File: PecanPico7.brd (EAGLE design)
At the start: 34.2 x 50 mm, 178 parts, among them IC1 Si4060-B1B-FM, IC10 TPS62260DRVT, IC11 TPS62261DRVT, IC12 TPS63021, IC13 RF6886, IC14 TPS78227DDCR, IC16 PAC1720-1-AIA-TR, IC2 Si4060-B1B-FM, IC3 BME280_BME280, IC4 uBlox MAX7/8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

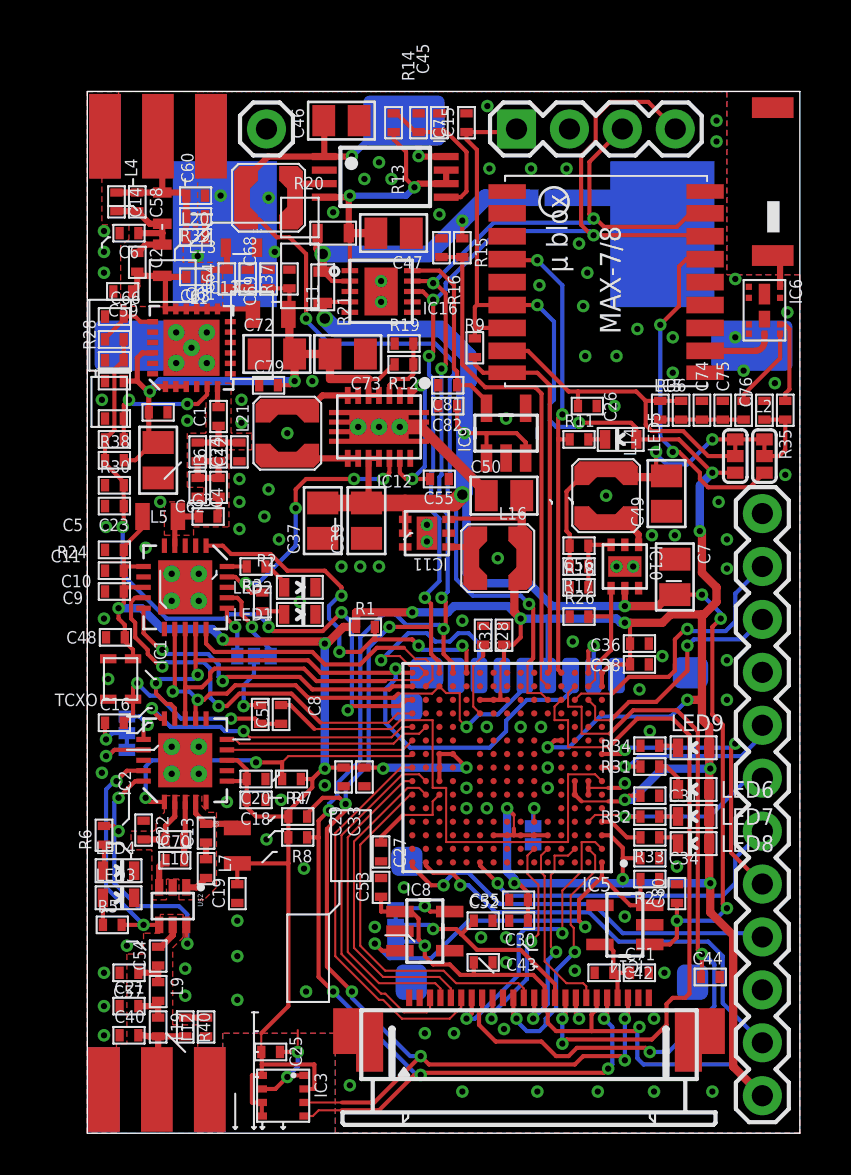
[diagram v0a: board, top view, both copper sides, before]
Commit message: Replaced small TCXO package to larger one
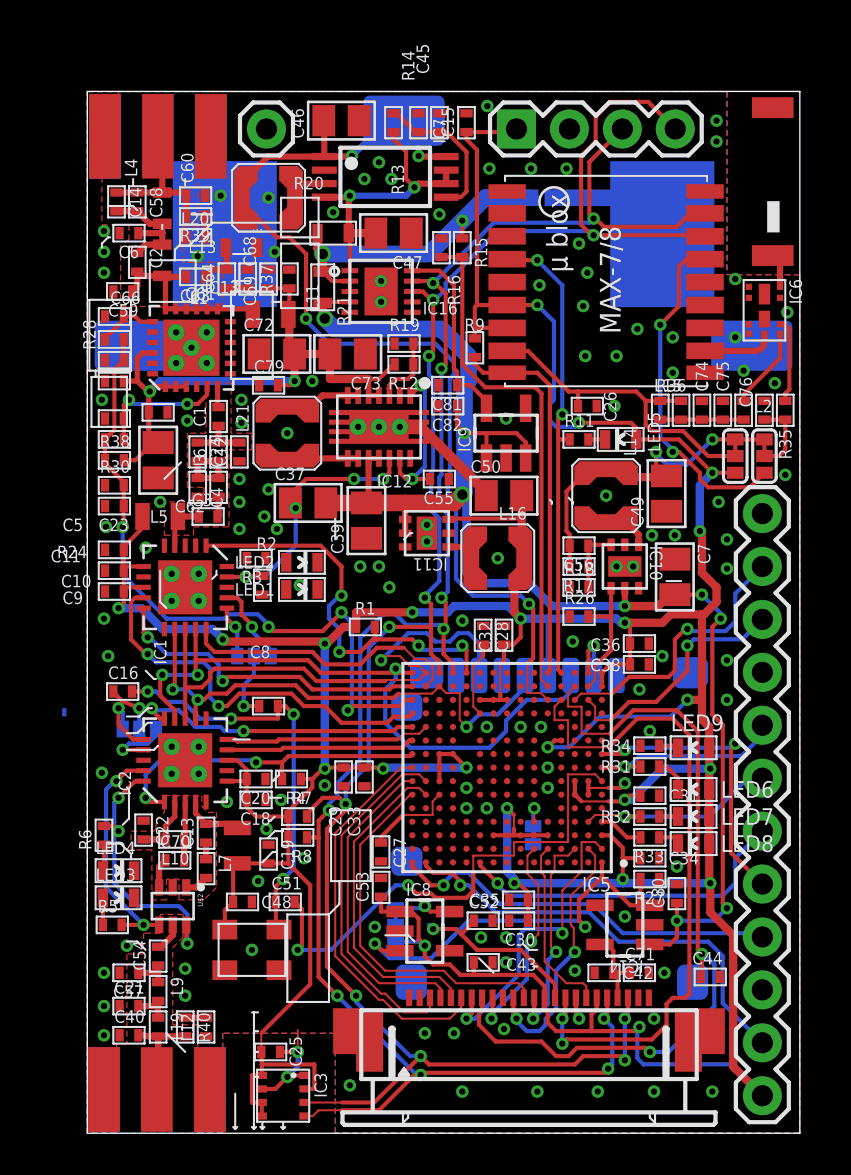
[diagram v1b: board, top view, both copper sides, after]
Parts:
- removed TCXO: KT2016K2BCW18ZAS, PecanFemto3:TCXO_2.0X1.6
- added U$3: TXC_7Z7Q, PecanFemto3:TCXO_3.2X2.5
- moved C48 14.1 mm to (7.45, 11.1), turned to 0 degrees
- moved C51 9.00 mm to (9.50, 11.1), turned to 0 degrees
- moved C19 2.42 mm to (8.70, 13.4), turned to 270 degrees
- moved C16 1.55 mm to (1.70, 21.2)
- moved LED1 1.20 mm to (10.3, 26.1)
- moved LED2 1.20 mm to (10.3, 27.4)
- moved C37 1.10 mm to (10.6, 30.2), turned to 0 degrees
- moved R2 0.80 mm to (8.40, 26.3)
- moved SJ6 0.63 mm to (2.50, 19.4), turned to 180 degrees
- moved C8 0.57 mm to (8.70, 20.5), turned to 0 degrees
- moved R3 0.40 mm to (8.10, 27.6)
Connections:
- net CLOCK: now also U$3.3; no longer TCXO.3
- net GND: now also U$3.1, U$3.2; no longer TCXO.1, TCXO.2
- net VCC: now also U$3.4; no longer TCXO.4
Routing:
- net CLOCK: track 9.88 -> 19.9 mm, vias 2 -> 4
- net CAM_VCC_CORE: track 10.4 -> 8.78 mm
- net N$22: track 1.46 -> 0.00 mm
- net N$19: track 1.95 -> 3.37 mm
- net N$21: track 1.20 -> 0.00 mm
- net N$13: track 0.95 -> 0.00 mm
- net N$39: track 25.3 -> 24.5 mm, vias 0 -> 2
- net VCC: track 250.2 -> 250.9 mm
- net RADIO1_SDN: track 19.4 -> 19.9 mm
- net N$34: track 1.94 -> 2.52 mm
- net PA_EN: track 13.5 -> 13.0 mm
- net GND: vias 123 -> 120

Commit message: Moved parts around
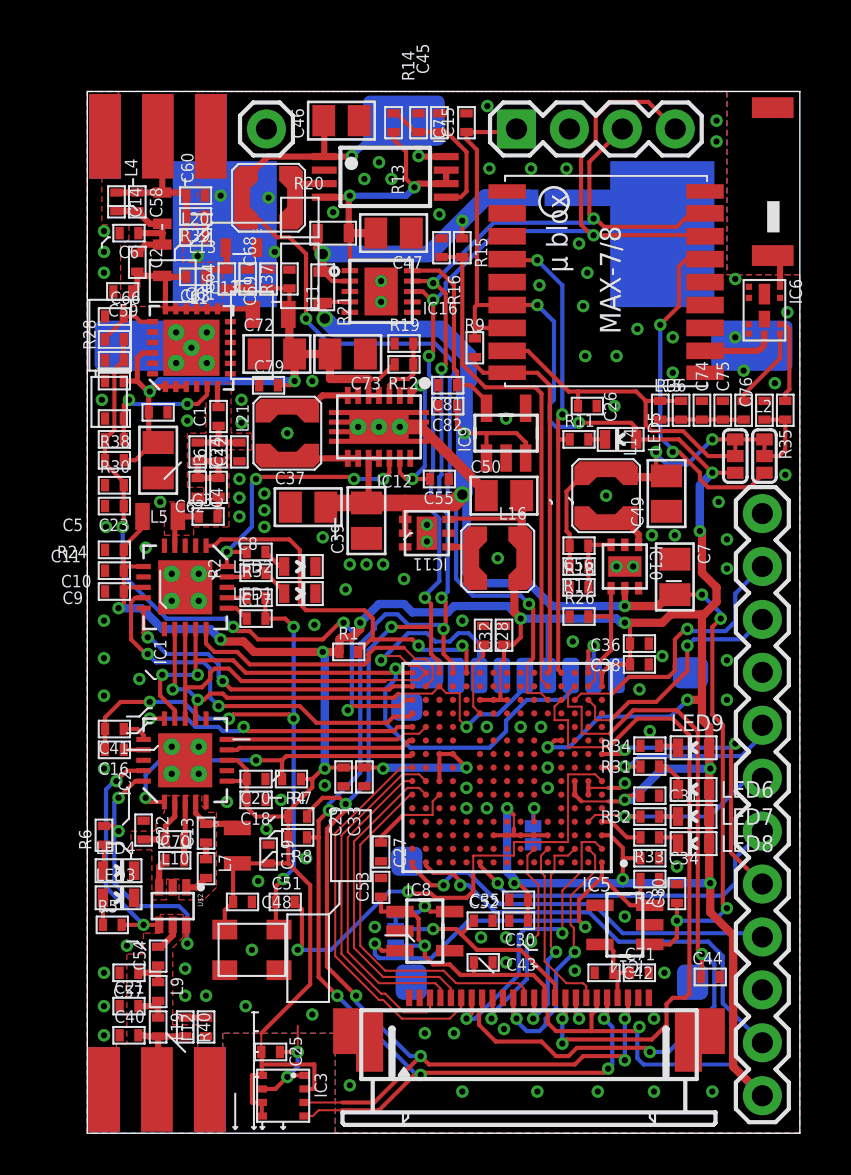
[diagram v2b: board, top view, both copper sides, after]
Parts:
- removed SJ5, SJ6: (no value), PecanPico6:SJ_2
- added C17, C41: 100pF, PecanPico6:0402
- moved C8 5.23 mm to (8.10, 25.7)
- moved C16 2.83 mm to (1.30, 18.4), turned to 180 degrees
- moved R1 1.44 mm to (12.6, 23.1)
- moved R2 0.67 mm to (8.10, 26.9), turned to 180 degrees
- moved R3 0.30 mm to (8.10, 27.9)
- moved LED1 0.22 mm to (10.2, 25.9)
- moved LED2 0.22 mm to (10.2, 27.2)
- moved C37 0.20 mm to (10.6, 30.1)
- moved SJ4 0.20 mm to (14.8, 9.80)
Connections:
- removed net N$34: C16.P$1, SJ6.2
- removed net N$8: IC1.17, SJ5.3
- net CLOCK: now also C17.P$2, C41.P$2
- net N$13: now also IC1.19, R2.P$2; no longer IC1.20, R3.P$2
- net N$18: now also C16.P$1; no longer SJ6.3
- net N$19: now also C41.P$1; no longer SJ6.1
- net N$37: now also IC1.17; no longer SJ5.2
- net N$9: now also C17.P$1; no longer SJ5.1
- net PA_EN: now also IC1.20, R3.P$2; no longer IC1.19, R2.P$2
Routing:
- net CLOCK: track 19.9 -> 29.0 mm, vias 4 -> 5
- net N$8: track 3.96 -> 0.00 mm, vias 1 -> 0
- net N$34: track 2.52 -> 0.00 mm, vias 1 -> 0
- net N$37: track 3.36 -> 0.95 mm, vias 1 -> 0
- net N$18: track 3.19 -> 0.95 mm, vias 1 -> 0
- net N$19: track 3.37 -> 1.27 mm, vias 1 -> 0
- net CAM_VCC_CORE: track 8.78 -> 10.3 mm
- net N$21: track 0.00 -> 1.37 mm
- net N$9: track 2.51 -> 1.16 mm, vias 1 -> 0
- net N$22: track 0.00 -> 1.19 mm
- net N$13: track 0.00 -> 1.15 mm
- net RADIO1_SDN: track 19.9 -> 19.1 mm, vias 4 -> 2
- net RADIO1_VREG_SW: track 32.6 -> 32.0 mm
- net GND: track 15.7 -> 15.9 mm, vias 120 -> 128

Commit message: Connected radio GPIOs to one UART TX
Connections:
- net RADIO2_GPIO1: now also IC5.C11; no longer IC5.L14
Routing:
- net RADIO2_GPIO1: track 9.80 -> 16.3 mm
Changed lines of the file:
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@@
 <signal name="RADIO2_GPIO1">
 <contactref element="IC2" pad="10"/>
-<contactref element="IC5" pad="L14"/>
-<wire x1="15.175" y1="19.175" x2="15.925" y2="19.175" width="0.1" layer="1"/>
-<wire x1="15.925" y1="19.175" x2="16.25" y2="19.5" width="0.1" layer="1"/>
 <wire x1="15.175" y1="19.175" x2="14.9" y2="18.9" width="0.1" layer="1"/>
 <wire x1="14.9" y1="18.9" x2="6.7" y2="18.9" width="0.2" layer="1"/>
+<wire x1="15.175" y1="19.175" x2="16.575" y2="19.175" width="0.1" layer="1"/>
+<wire x1="16.575" y1="19.175" x2="16.575" y2="16.575" width="0.1" layer="1"/>
+<wire x1="16.575" y1="16.575" x2="17.225" y2="16.575" width="0.1" layer="1"/>
+<wire x1="17.225" y1="16.575" x2="17.225" y2="14.625" width="0.1" layer="1"/>
+<contactref element="IC5" pad="C11"/>
+<wire x1="17.225" y1="14.625" x2="17.875" y2="14.625" width="0.1" layer="1"/>
+<wire x1="17.875" y1="14.625" x2="18.2" y2="14.3" width="0.1" layer="1"/>
 </signal>
 <signal name="RADIO2_CS">

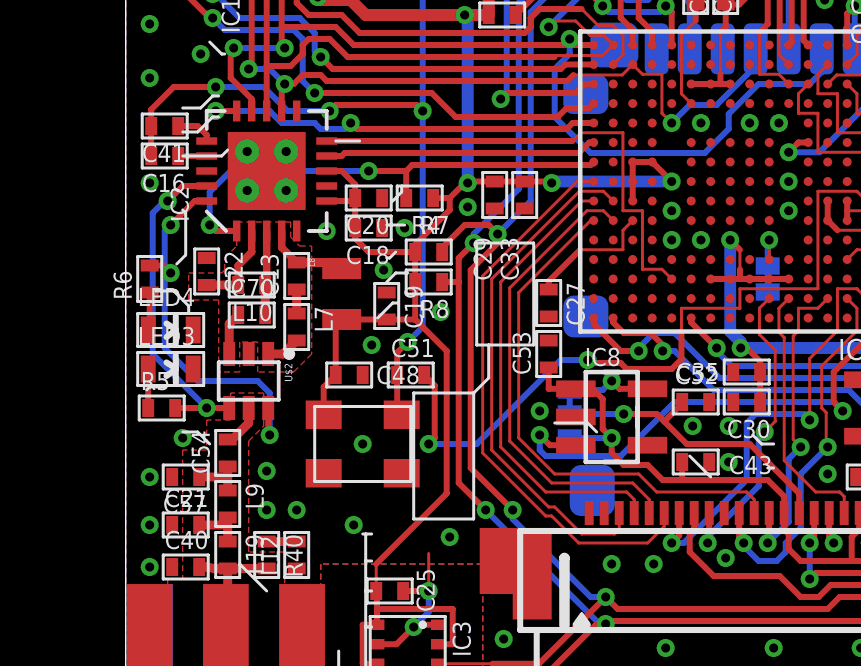
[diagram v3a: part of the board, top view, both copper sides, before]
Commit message: Moved parts around
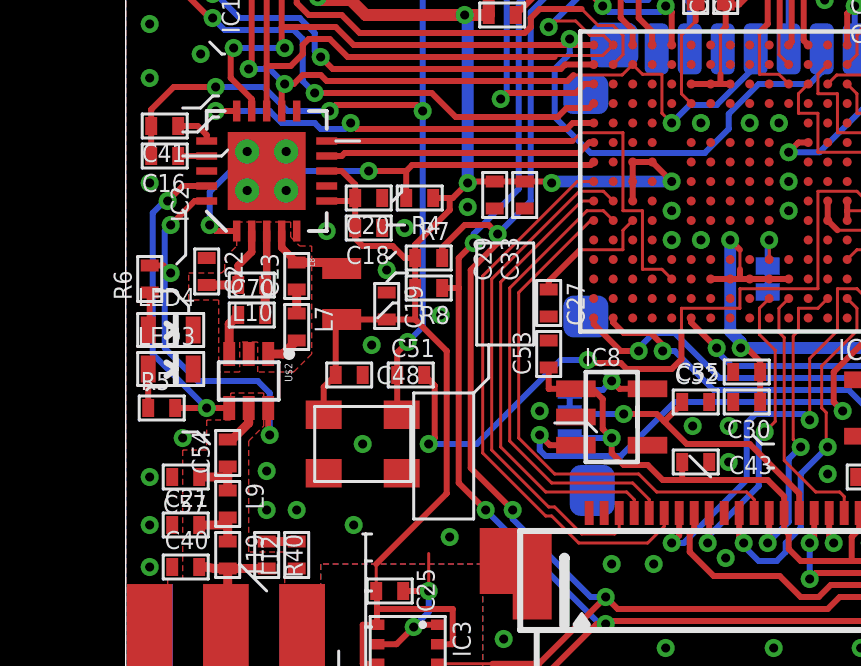
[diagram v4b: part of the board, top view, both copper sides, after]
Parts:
- moved R7 0.20 mm to (10.1, 15.0)
- moved R8 0.20 mm to (10.1, 14.0)
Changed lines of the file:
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@@
 <text x="14.3" y="13.5" size="0.7" layer="38" rot="MR270">1.3V</text>
 <text x="14.3" y="8.4" size="0.7" layer="38" rot="MR270">1.8V</text>
-<text x="9.1" y="22" size="0.7" layer="38" rot="MR270">XIN</text>
-<text x="7.5" y="22.1" size="0.7" layer="38" rot="MR270">XOUT</text>
-<text x="2.8" y="18.7" size="0.7" layer="38" rot="MR180">XIN</text>
-<text x="2.8" y="20.3" size="0.7" layer="38" rot="MR180">XOUT</text>
+<text x="-4.1" y="21.5" size="0.7" layer="38" rot="MR180">XIN</text>
+<text x="-5" y="22.9" size="0.7" layer="38" rot="MR180">XOUT</text>
+<text x="-3.8" y="18.5" size="0.7" layer="38" rot="MR180">XIN</text>
+<text x="-4.9" y="19.8" size="0.7" layer="38" rot="MR180">XOUT</text>
 <wire x1="23.6" y1="46.8" x2="23.6" y2="43.8" width="0.2" layer="38"/>
 <wire x1="23.6" y1="43.8" x2="22.8" y2="43" width="0.2" layer="38"/>
@@
 <attribute name="VALUE" x="8.2" y="-0.2" size="0.6" layer="27"/>
 </element>
-<element name="R7" library="PecanPico6" package="0402" value="10k" x="10.1" y="15.2" smashed="yes" rot="R180">
-<attribute name="NAME" x="10.8" y="16.4" size="0.6" layer="25" rot="R180"/>
-<attribute name="VALUE" x="10.8" y="16.4" size="0.6" layer="27" rot="R180"/>
-</element>
-<element name="R8" library="PecanPico6" package="0402" value="10k" x="10.1" y="14.2" smashed="yes" rot="R180">
-<attribute name="NAME" x="10.8" y="13.6" size="0.6" layer="25" rot="R180"/>
-<attribute name="VALUE" x="10.8" y="15.4" size="0.6" layer="27" rot="R180"/>
+<element name="R7" library="PecanPico6" package="0402" value="10k" x="10.1" y="15" smashed="yes" rot="R180">
+<attribute name="NAME" x="10.8" y="16.2" size="0.6" layer="25" rot="R180"/>
+<attribute name="VALUE" x="10.8" y="16.2" size="0.6" layer="27" rot="R180"/>
+</element>
+<element name="R8" library="PecanPico6" package="0402" value="10k" x="10.1" y="14" smashed="yes" rot="R180">
+<attribute name="NAME" x="10.8" y="13.4" size="0.6" layer="25" rot="R180"/>
+<attribute name="VALUE" x="10.8" y="15.2" size="0.6" layer="27" rot="R180"/>
 </element>
 <element name="C25" library="PecanPico6" package="0402" value="100nF" x="8.8" y="3.9" smashed="yes" rot="R180">
@@
 <via x="6.4" y="45" extent="1-16" drill="0.3"/>
 <via x="11.8" y="44.2" extent="1-16" drill="0.3"/>
-<via x="8.6" y="14.6" extent="1-16" drill="0.3"/>
+<via x="8.7" y="14.6" extent="1-16" drill="0.3"/>
 <contactref element="IC12" pad="2"/>
 <contactref element="R19" pad="P$1"/>
@@
 <vertex x="3.8" y="11.2"/>
 </polygon>
-<via x="10.5" y="13.2" extent="1-16" drill="0.3"/>
+<via x="10.5" y="13.1" extent="1-16" drill="0.3"/>
 <via x="7.9" y="8.8" extent="1-16" drill="0.3"/>
 <via x="19.7" y="27.6" extent="1-16" drill="0.3"/>
@@
 <wire x1="11.4" y1="23" x2="11.4" y2="17.5" width="0.4" layer="16"/>
 <wire x1="7.65" y1="16" x2="7.65" y2="15.65" width="0.2" layer="1"/>
-<wire x1="7.65" y1="15.65" x2="8.1" y2="15.2" width="0.2" layer="1"/>
+<wire x1="7.65" y1="15.65" x2="7.9" y2="15.4" width="0.2" layer="1"/>
 <wire x1="25.8" y1="24.5" x2="26.05" y2="24.5" width="0.4" layer="1"/>
 <wire x1="26.05" y1="24.5" x2="27.6" y2="24.5" width="0.4" layer="1"/>
@@
 <wire x1="28" y1="24.9" x2="29.5" y2="24.9" width="0.4" layer="1"/>
 <wire x1="26.05" y1="23.5" x2="26.05" y2="24.5" width="0.2" layer="1"/>
-<wire x1="9.65" y1="14.2" x2="9.65" y2="15.2" width="0.2" layer="1"/>
-<wire x1="8.1" y1="15.2" x2="9.65" y2="15.2" width="0.2" layer="1"/>
-<wire x1="9.65" y1="15.2" x2="9.65" y2="15.45" width="0.2" layer="1"/>
+<wire x1="9.65" y1="14" x2="9.65" y2="15" width="0.2" layer="1"/>
+<wire x1="7.9" y1="15.4" x2="8.9" y2="15.4" width="0.2" layer="1"/>
+<wire x1="8.9" y1="15.4" x2="9.3" y2="15" width="0.2" layer="1"/>
+<wire x1="9.3" y1="15" x2="9.65" y2="15" width="0.2" layer="1"/>
+<wire x1="9.65" y1="15" x2="9.65" y2="15.45" width="0.2" layer="1"/>
 <wire x1="8.375" y1="1.475" x2="7.9" y2="1.475" width="0.2" layer="1"/>
 <wire x1="7.9" y1="1.475" x2="7.9" y2="2.775" width="0.2" layer="1"/>
@@
 <wire x1="12.3" y1="17.55" x2="11.45" y2="17.55" width="0.2" layer="1"/>
 <wire x1="11.45" y1="17.55" x2="11.4" y2="17.5" width="0.2" layer="1"/>
-<wire x1="11.4" y1="17.5" x2="11.3" y2="17.5" width="0.2" layer="1"/>
-<wire x1="11.3" y1="17.5" x2="10.8" y2="17" width="0.2" layer="1"/>
 <wire x1="10.8" y1="17" x2="10.8" y2="16.6" width="0.2" layer="1"/>
 <wire x1="10.8" y1="16.6" x2="9.65" y2="15.45" width="0.2" layer="1"/>
@@
 <wire x1="30.9" y1="3.3" x2="32.4" y2="1.8" width="0.2" layer="16"/>
 <wire x1="29.9" y1="10.6" x2="31" y2="9.5" width="0.4" layer="1"/>
-<wire x1="9.65" y1="14.2" x2="9.65" y2="12.95" width="0.2" layer="1"/>
+<wire x1="9.65" y1="14" x2="9.65" y2="12.95" width="0.2" layer="1"/>
 <wire x1="15.0062" y1="10.6398" x2="15.5602" y2="10.6398" width="0.2" layer="1"/>
 <wire x1="15.5602" y1="10.6398" x2="15.9" y2="10.3" width="0.2" layer="1"/>
@@
 <wire x1="12.7" y1="23.8" x2="13.1" y2="24.2" width="0.4" layer="1"/>
 <wire x1="13.1" y1="24.2" x2="13.1" y2="24.5" width="0.4" layer="1"/>
+<wire x1="11.4" y1="17.5" x2="10.9" y2="17" width="0.2" layer="1"/>
+<wire x1="10.9" y1="17" x2="10.8" y2="17" width="0.2" layer="1"/>
 </signal>
 <signal name="RADIO2_SDN">
@@
 <wire x1="25.6" y1="3.7" x2="25.8" y2="3.5" width="0.2" layer="1"/>
 <via x="14.6" y="24.3" extent="1-16" drill="0.3"/>
-<wire x1="10.55" y1="15.2" x2="10.55" y2="15.35" width="0.2" layer="1"/>
+<wire x1="10.55" y1="15" x2="10.55" y2="15.35" width="0.2" layer="1"/>
 <wire x1="10.55" y1="15.35" x2="11.3" y2="16.1" width="0.2" layer="1"/>
 <wire x1="11.3" y1="16.1" x2="12.1" y2="16.1" width="0.2" layer="1"/>
@@
 <via x="11.6" y="15.5" extent="1-16" drill="0.3"/>
 <wire x1="11.6" y1="15.5" x2="11.1" y2="15" width="0.2" layer="1"/>
-<wire x1="11.1" y1="15" x2="11.1" y2="14.2" width="0.2" layer="1"/>
+<wire x1="11.1" y1="15" x2="11.1" y2="14" width="0.2" layer="1"/>
 <via x="12" y="6.6" extent="1-16" drill="0.3"/>
 <wire x1="24.8" y1="2.9" x2="25" y2="3.1" width="0.2" layer="1"/>
 <via x="25" y="3.1" extent="1-16" drill="0.3"/>
-<wire x1="10.55" y1="14.2" x2="11.1" y2="14.2" width="0.2" layer="1"/>
+<wire x1="10.55" y1="14" x2="11.1" y2="14" width="0.2" layer="1"/>
 <wire x1="16.1" y1="2.9" x2="16" y2="2.8" width="0.2" layer="1"/>
 <via x="16" y="2.8" extent="1-16" drill="0.3"/>
@@
 <wire x1="17.3" y1="29.7" x2="17.3" y2="26" width="0.2" layer="16"/>
 <wire x1="17.3" y1="26" x2="17" y2="25.7" width="0.2" layer="16"/>
-<wire x1="11.1" y1="14.2" x2="11.1" y2="7.5" width="0.2" layer="1"/>
+<wire x1="11.1" y1="14" x2="11.1" y2="7.5" width="0.2" layer="1"/>
 <wire x1="16.9" y1="30.1" x2="16.9" y2="31.5" width="0.2" layer="16"/>
 <wire x1="16.9" y1="31.5" x2="17" y2="31.6" width="0.2" layer="16"/>
